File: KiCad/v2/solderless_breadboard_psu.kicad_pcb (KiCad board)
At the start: 4 copper layers, 53 x 51 mm, 78 parts, among them IC201 TPS63000DRCR, IC202 TPS63000DRCR, IC301 CP2102N-A02-GQFN24R, J201 Conn_01x02_Pin, J202 Conn_01x03_Pin, J203 Conn_02x03_Odd_Even, J204 Conn_01x03_Pin, J205 Conn_02x03_Odd_Even, J301 Conn_01x09_Pin, J302 Conn_01x09_Pin, J303 Conn_01x06_Pin, J304 USB_C_Receptacle_USB2.0_16P, J305 Conn_01x03_Pin, U301 USBLC6-2SC6

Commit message: First routing
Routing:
- net UART_VDD: track 19.9 -> 46.0 mm, vias 2 -> 3
- net VUSB_FILT: track 38.0 -> 62.8 mm, vias 2 -> 3
- net VCC_SEL: track 0.00 -> 20.6 mm
- net /[3] USB 2 UART/RXD: track 44.4 -> 33.8 mm
- net /[3] USB 2 UART/TXD: track 39.8 -> 32.9 mm
- net Net-(D304-A): track 0.00 -> 5.07 mm
- net /[3] USB 2 UART/DTR: track 45.1 -> 41.8 mm, vias 0 -> 1
- net GND: track 53.6 -> 56.2 mm, vias 109 -> 112
- net /[3] USB 2 UART/SUSPEND: track 26.9 -> 28.7 mm
- net /[3] USB 2 UART/RTS: track 18.8 -> 20.1 mm, vias 1 -> 0
- net /[3] USB 2 UART/DSR: track 11.3 -> 10.4 mm, vias 1 -> 0
- net /[3] USB 2 UART/RSTB: track 10.9 -> 10.1 mm
- net /[3] USB 2 UART/VBUS: track 14.2 -> 13.6 mm
- net /[3] USB 2 UART/CTS: track 21.1 -> 21.0 mm, vias 1 -> 0

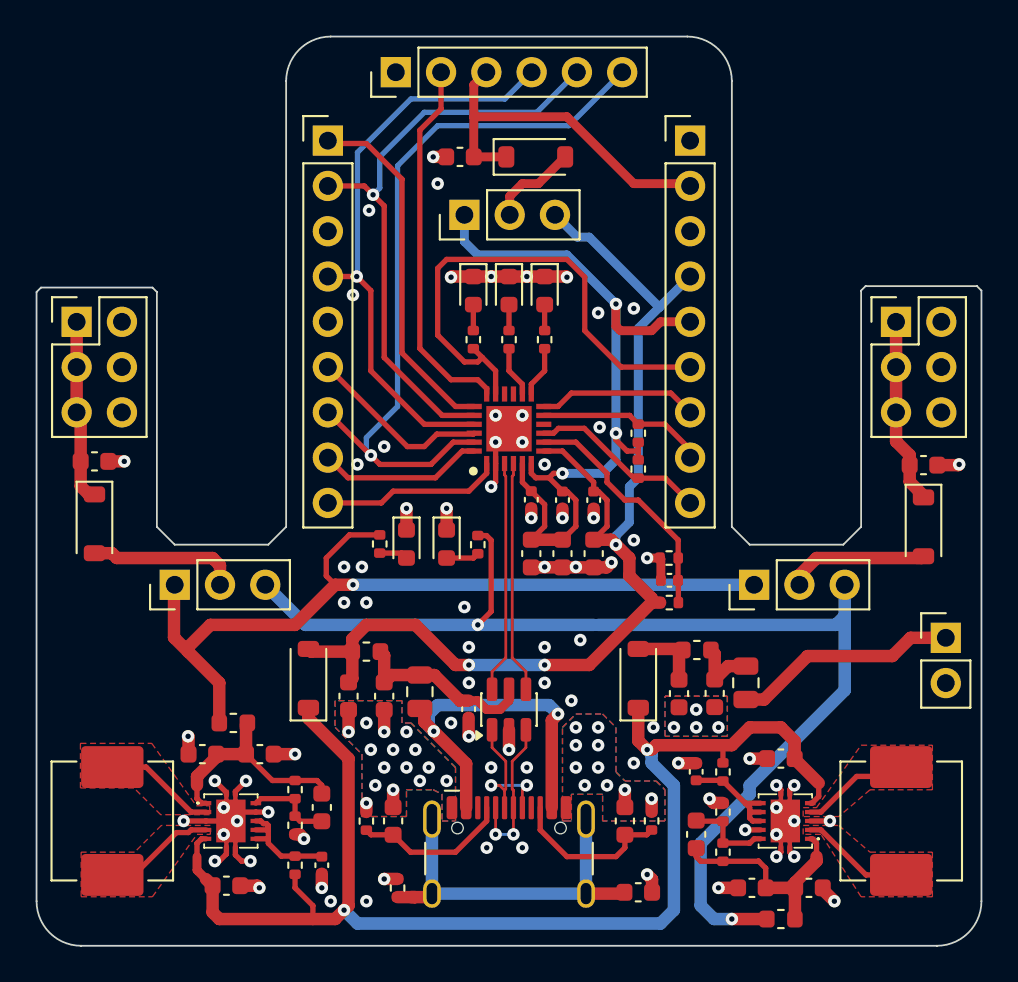
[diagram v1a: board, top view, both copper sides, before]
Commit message: silkscreen updates
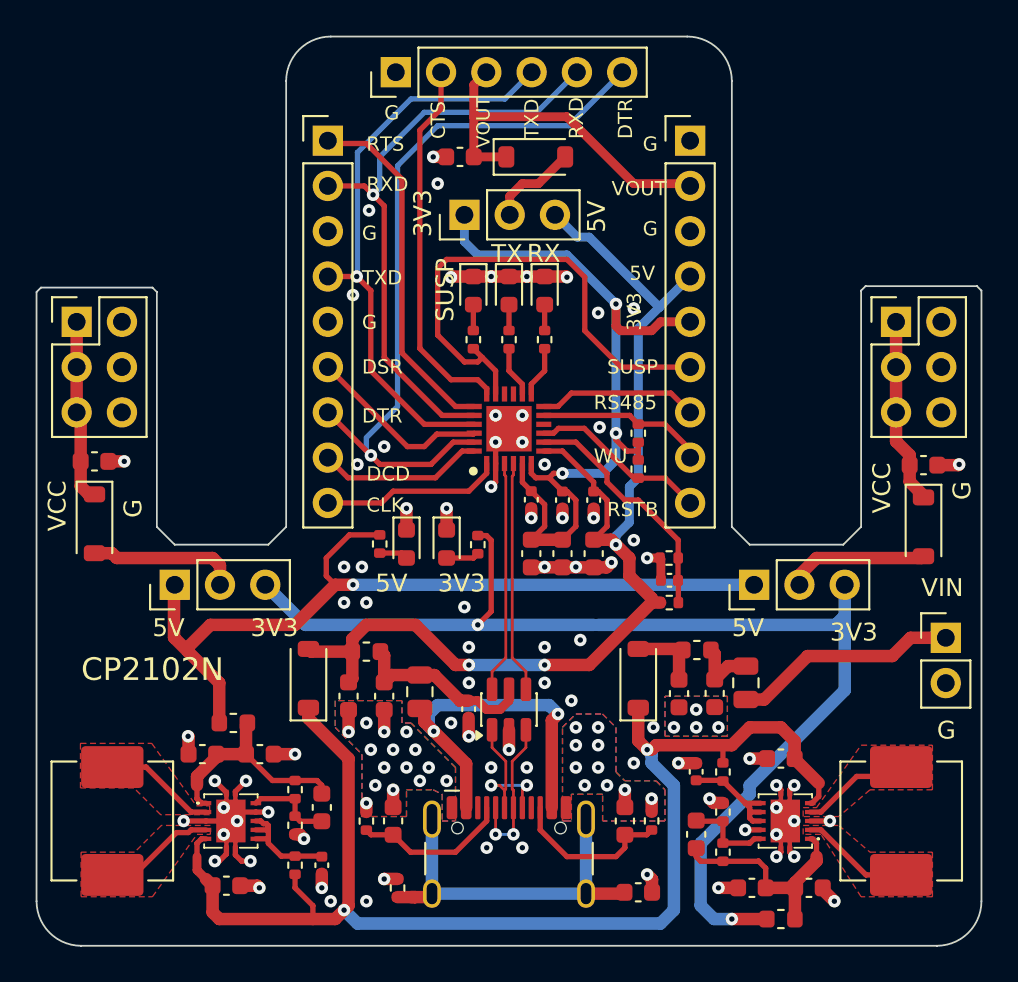
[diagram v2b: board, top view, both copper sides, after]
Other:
- board text added: "3V3"
- board text added: "5V"
- board text added: "CLK"
- board text added: "CP2102N"
- board text added: "CTS"
- board text added: "DCD"
- board text added: "DSR"
- board text added: "DTR"
- board text added: "G"
- board text added: "RS485"
- board text added: "RSTB"
- board text added: "RTS"
- board text added: "RX"
- board text added: "RXD"
- board text added: "SUSP"
- board text added: "TX"
- board text added: "TXD"
- board text added: "VCC"
- board text added: "VIN"
- board text added: "VOUT"
- board text added: "WU"
